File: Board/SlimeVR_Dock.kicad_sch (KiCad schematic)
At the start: 24 parts, among them J1_Control Conn_01x03_Pin, J1_MainPW USB_C_Receptacle_USB2.0_16P, J1_Prog Conn_01x03_Pin, M1 NF-A4x10 24V PWM, Q1 AO3401A, U1 ESP32-S3-WROOM-1, U2 CH224K, U3 XC6220B331MR, U4 DS18B20

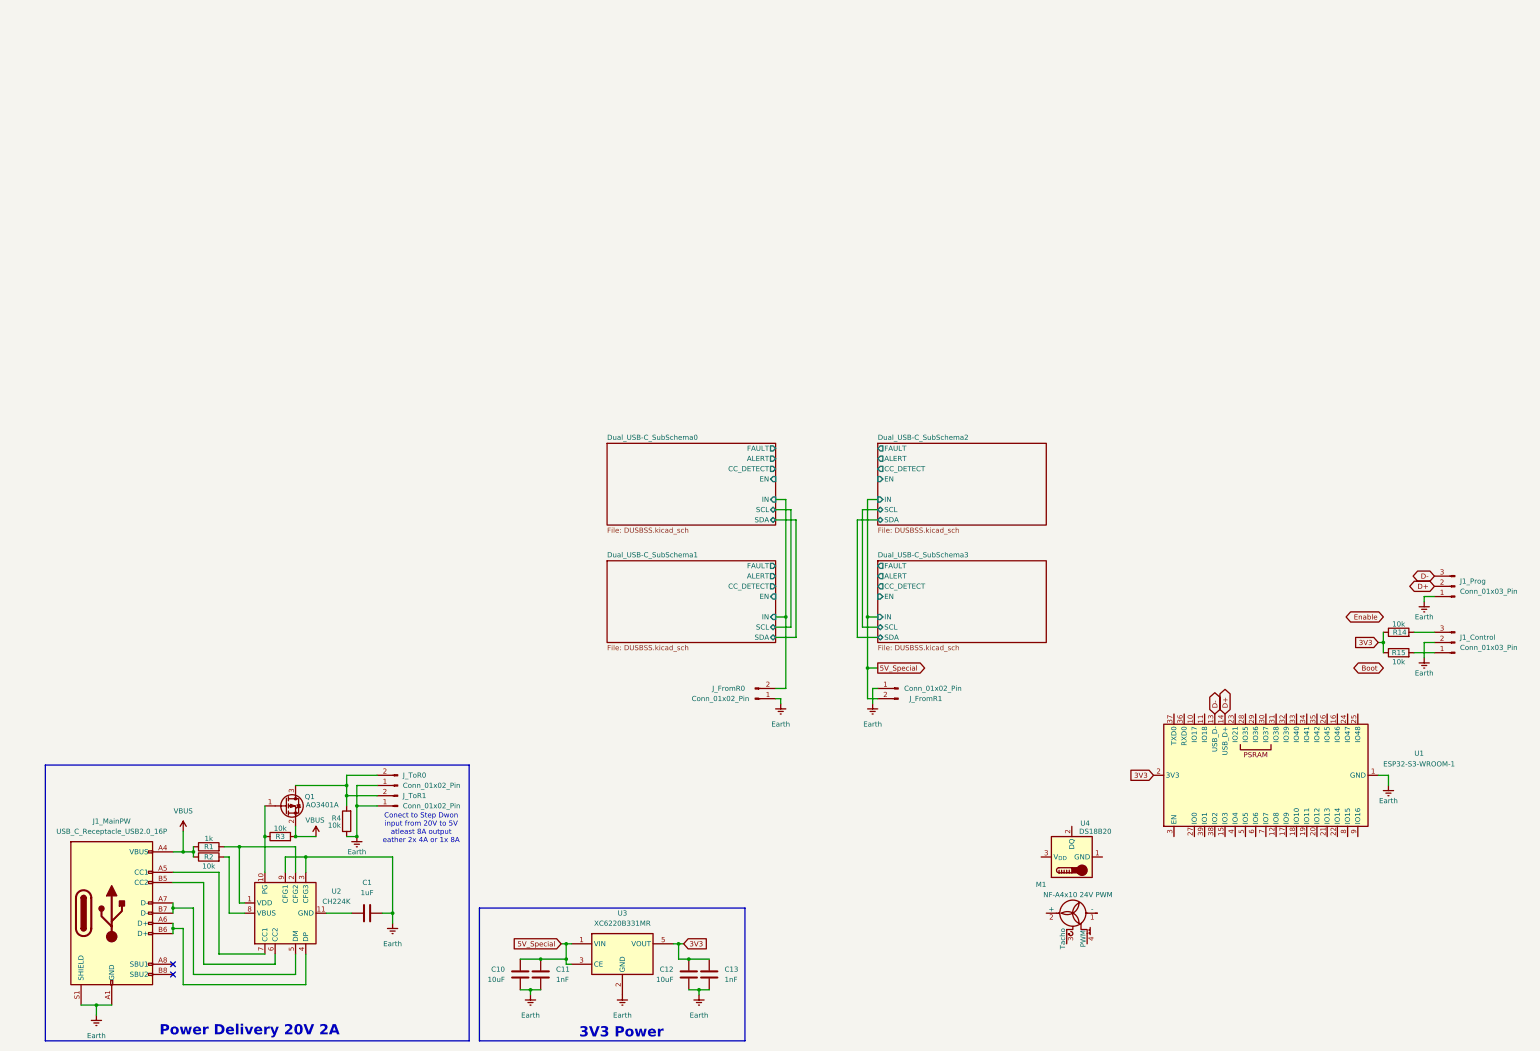
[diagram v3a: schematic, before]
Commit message: Conecting usb to esp
added in/out and out/in reistry
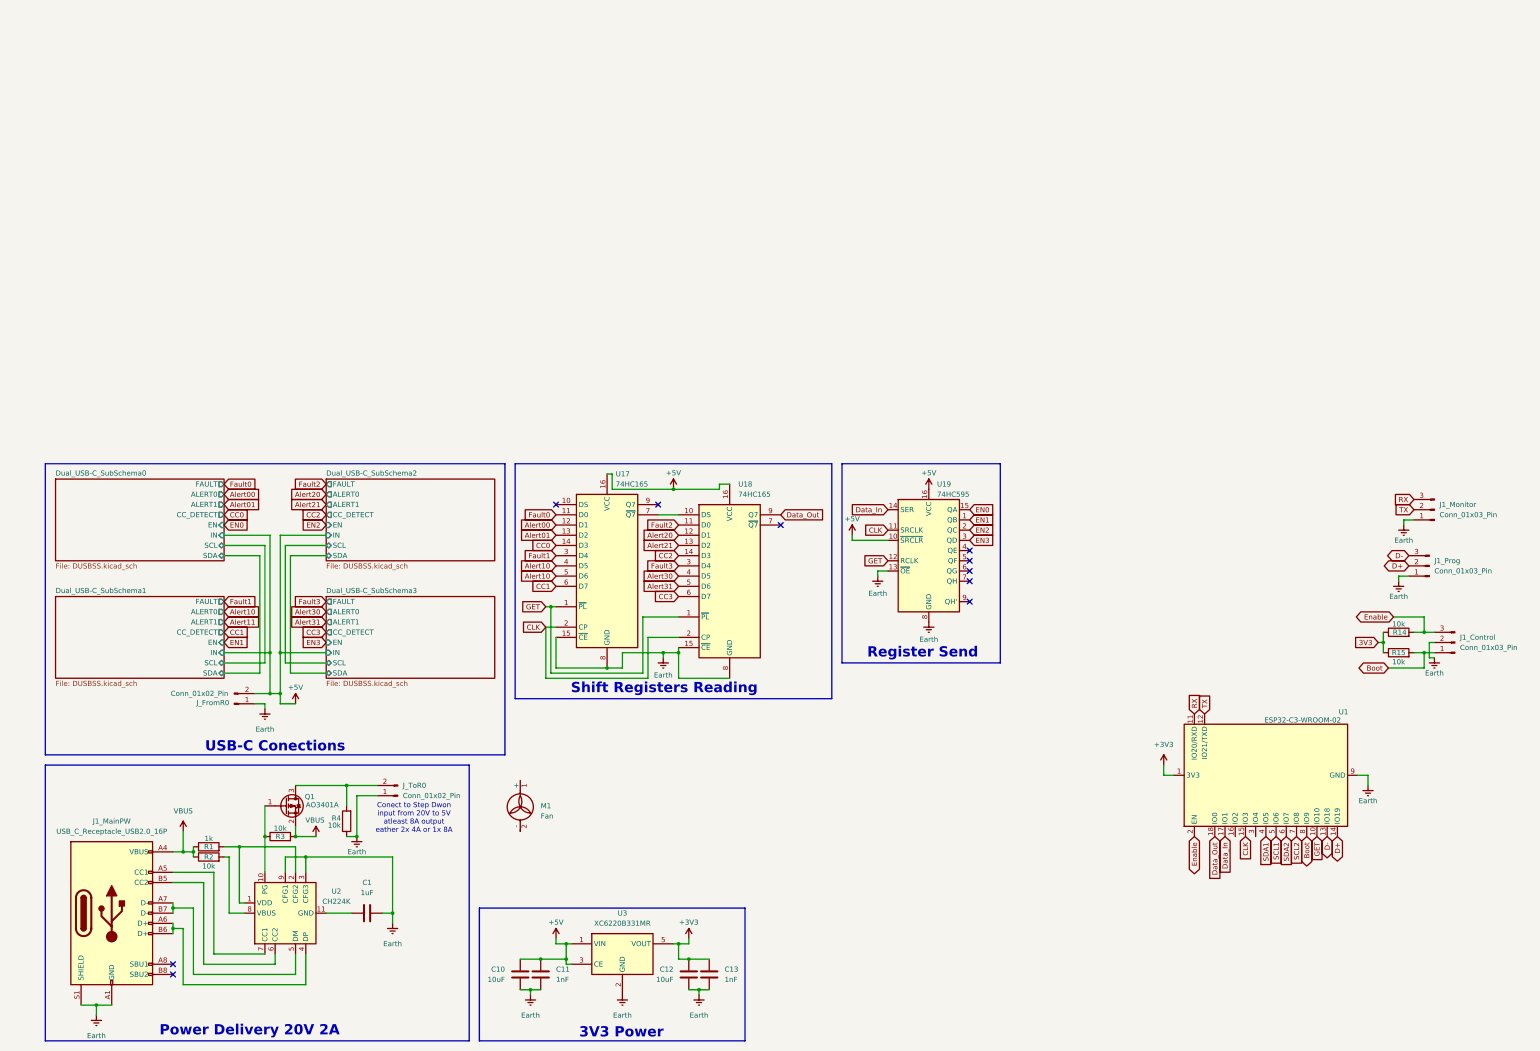
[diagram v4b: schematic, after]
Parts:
- removed J_FromR0, J_ToR1: Conn_01x02_Pin, symbol Connector:Conn_01x02_Pin
- removed M1: NF-A4x10 24V PWM, symbol Motor:Fan_4pin
- removed U1: ESP32-S3-WROOM-1, RF_Module:ESP32-S3-WROOM-1, symbol RF_Module:ESP32-S3-WROOM-1
- removed U4: DS18B20, Package_TO_SOT_THT:TO-92_Inline, symbol Sensor_Temperature:DS18B20
- added J1_Monitor: Conn_01x03_Pin, symbol Connector:Conn_01x03_Pin
- added M1: Fan, symbol Motor:Fan
- added U1: ESP32-C3-WROOM-02, RF_Module:ESP32-C3-WROOM-02, symbol RF_Module:ESP32-C3-WROOM-02
- added U17, U18: 74HC165, symbol 74xx:74HC165
- added U19: 74HC595, symbol 74xx:74HC595
- renumbered J_FromR1 to J_FromR0
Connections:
- net 3V3: no longer C12.1, C13.1, U3.5 (VOUT)
- net Boot: now also J1_Control.1 (Pin_1), R15.2, U1.8 (IO9)
- net D+: now also U1.14 (IO19)
- net D-: now also U1.13 (IO18)
- net Earth: now also J1_Monitor.1 (Pin_1), U1.19 (GND), U1.9 (GND), U17.15 (~{CE}), U17.8 (GND), U18.15 (~{CE}), U18.8 (GND), U19.13 (~{OE}), U19.8 (GND)
- net Enable: now also J1_Control.3 (Pin_3), R14.2, U1.2 (EN)
- net 5V_Special renamed +5V
- net +5V: now also U17.16 (VCC), U18.16 (VCC), U19.10 (~{SRCLR}), U19.16 (VCC)
- new net: U17.7 (~{Q7}), U18.10 (DS)
- new net +3V3: C12.1, C13.1, U1.1 (3V3), U3.5 (VOUT)
- new net Alert00: U17.12 (D1)
- new net Alert01: U17.13 (D2)
- new net Alert10: U17.4 (D5), U17.5 (D6)
- new net Alert20: U18.12 (D1)
- new net Alert21: U18.13 (D2)
- new net Alert30: U18.4 (D5)
- new net Alert31: U18.5 (D6)
- new net CC0: U17.14 (D3)
- new net CC1: U17.6 (D7)
- new net CC2: U18.14 (D3)
- new net CC3: U18.6 (D7)
- new net CLK: U1.15 (IO3), U17.2 (CP), U18.2 (CP), U19.11 (SRCLK)
- new net Data_In: U1.17 (IO1), U19.14 (SER)
- new net Data_Out: U1.18 (IO0), U18.9 (Q7)
- new net EN0: U19.15 (QA)
- new net EN1: U19.1 (QB)
- new net EN2: U19.2 (QC)
- new net EN3: U19.3 (QD)
- new net Fault0: U17.11 (D0)
- new net Fault1: U17.3 (D4)
- new net Fault2: U18.11 (D0)
- new net Fault3: U18.3 (D4)
- new net GET: U1.10 (IO10), U17.1 (~{PL}), U18.1 (~{PL}), U19.12 (RCLK)
- new net RX: J1_Monitor.3 (Pin_3), U1.11 (IO20/RXD)
- new net SCL1: U1.5 (IO6)
- new net SCL2: U1.7 (IO8)
- new net SDA1: U1.4 (IO5)
- new net SDA2: U1.6 (IO7)
- new net TX: J1_Monitor.2 (Pin_2), U1.12 (IO21/TXD)
- no-connect marks 2 -> 10
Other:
- sheet Dual_USB-C_SubSchema0 ports: added ALERT0, ALERT1; removed ALERT
- sheet Dual_USB-C_SubSchema1 ports: added ALERT0, ALERT1; removed ALERT
- sheet Dual_USB-C_SubSchema2 ports: added ALERT0, ALERT1; removed ALERT
- sheet Dual_USB-C_SubSchema3 ports: added ALERT0, ALERT1; removed ALERT
- note added: "Register Send"
- note added: "Shift Registers Reading"
- note added: "USB-C Conections"
- moved on the sheet: J1_Prog, J_FromR0, J_ToR0

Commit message: Finished Schematic
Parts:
- removed M1: Fan, symbol Motor:Fan
- added JFan1: Conn_01x04_Pin, Connector:FanPinHeader_1x04_P2.54mm_Vertical, symbol Connector:Conn_01x04_Pin
- added R23, R24: 4.7k, Resistor_SMD:R_0603_1608Metric, symbol Device:R
- C1, C10, C11, C12, C13: footprint (none) -> Capacitor_SMD:C_0603_1608Metric
- J1_Control1: renamed from J1_Control; footprint (none) -> Connector_PinHeader_2.54mm:PinHeader_1x03_P2.54mm_Vertical
- J1_MainPW1: renamed from J1_MainPW; footprint (none) -> Connector_USB:USB_C_Receptacle_GCT_USB4105-xx-A_16P_TopMnt_Horizontal
- J1_Monitor1: renamed from J1_Monitor; footprint (none) -> Connector_PinHeader_2.54mm:PinHeader_1x03_P2.54mm_Vertical
- J1_Prog1: renamed from J1_Prog; footprint (none) -> Connector_PinHeader_2.54mm:PinHeader_1x03_P2.54mm_Vertical
- J_FromR0, J_ToR0: footprint (none) -> Connector_PinHeader_2.54mm:PinHeader_1x02_P2.54mm_Vertical
- R1, R2, R3, R4: footprint (none) -> Resistor_SMD:R_0603_1608Metric
- R17: renamed from R14; footprint (none) -> Resistor_SMD:R_0603_1608Metric
- R18: renamed from R15; footprint (none) -> Resistor_SMD:R_0603_1608Metric
- U17, U18, U19: footprint (none) -> Package_SO:SOIC-16_3.9x9.9mm_P1.27mm
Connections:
- net 3V3 is gone; now on net +3V3: R17.1, R18.1
- net SDA1 is gone; now on net CLK: U1.4 (IO5)
- net +3V3: now also U17.16 (VCC), U18.16 (VCC), U19.16 (VCC), R23.2, R24.1
- net +5V: now also JFan1.2 (Pin_2); no longer U17.16 (VCC), U18.16 (VCC), U19.16 (VCC)
- net CLK: no longer U1.15 (IO3)
- net Earth: now also C1.1, U2.11 (GND), JFan1.1 (Pin_1); no longer C1.2
- net SCL: now reaches U1.3 (IO4)
- net SCL: now also R23.1
- net at R1.2, U2.1 (VDD), U2.2 (CFG2): now also C1.2
- net SCL1 renamed TACH
- net TACH: now also JFan1.3 (Pin_3)
- net SCL2: no longer names the net of U1.7 (IO8)
- net SDA2 renamed PWM
- net PWM: now also JFan1.4 (Pin_4)
- new net SDA: R24.2, U1.15 (IO3)
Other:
- sheet Dual_USB-C_SubSchema0 ports: added A00, A01, A10, A11; removed none
- sheet Dual_USB-C_SubSchema1 ports: added A00, A01, A10, A11; removed none
- sheet Dual_USB-C_SubSchema2 ports: added A00, A01, A10, A11; removed none
- sheet Dual_USB-C_SubSchema3 ports: added A00, A01, A10, A11; removed none
- note added: "Conect to Step Dwon input from 20V to 5V atleast 8A+ output"
- note added: "Dev pins"
- note added: "I recomend XL4016, 9A"
- note added: "MCU"
- note added: "Power Delivery 20V 3A"
- note removed: "Conect to Step Dwon input from 20V to 5V atleast 8A output eather 2x 4A or 1x 8A"
- note removed: "Power Delivery 20V 2A"
- moved on the sheet: C1, C10, C11, C12, C13, J1_Control1, J1_MainPW1, J1_Monitor1, J1_Prog1, J_FromR0, J_ToR0, Q1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

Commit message: Updavení USB-C
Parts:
- added BZ1: Buzzer, Buzzer_Beeper:Buzzer_12x9.5RM7.6, symbol Device:Buzzer
- added D1: 1N4148, Diode_SMD:D_0603_1608Metric, symbol Device:D
- added J1Temp1: Conn_01x05_Pin, Connector_PinHeader_2.54mm:PinHeader_1x05_P2.54mm_Vertical, symbol Connector:Conn_01x05_Pin
- added Q6: BC817, Package_TO_SOT_SMD:SOT-23, symbol Transistor_BJT:BC817
- added R33: 1k, Resistor_SMD:R_0603_1608Metric, symbol Device:R
- renumbered JFan1 to J1Fan1
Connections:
- net +3V3: now also J1Temp1.1 (Pin_1)
- net +5V: now also BZ1.1 (+), D1.1 (K)
- net Earth: now also J1Temp1.3 (Pin_3), Q6.2 (E)
- net SCL: now also J1Temp1.2 (Pin_2)
- net SDA: now also J1Temp1.4 (Pin_4)
- net BZ: now reaches U19.4 (QE)
- net BZ: now also R33.1
- new net: Q6.1 (B), R33.2
- new net: BZ1.2 (-), D1.2 (A), Q6.3 (C)
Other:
- note added: "3V3 Power Generator"
- note added: "I use TC74A0 in TO-220 footprint"
- note added: "Shift Register Send"
- note added: "StepDwon Fan Sensor Conector"
- note added: "Tempeture Sensor Conector"
- note added: "User Warning"
- note removed: "3V3 Power"
- note removed: "Register Send"
- moved on the sheet: J1Fan1

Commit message: Custom StepDown
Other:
- added sheet StepDown (StepDown.kicad_sch)
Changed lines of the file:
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@@
+	)
+	(sheet
+		(at 106.68 114.3)
+		(size 12.7 8.89)
+		(exclude_from_sim no)
+		(in_bom yes)
+		(on_board yes)
+		(dnp no)
+		(stroke
+			(width 0.1524)
+			(type solid)
+		)
+		(fill
+			(color 0 0 0 0.0000)
+		)
+		(property "Sheetname" "StepDown"
+			(at 106.68 113.5884 0)
+			(effects
+				(font
+					(size 1.27 1.27)
+				)
+				(justify left bottom)
+			)
+		)
+		(property "Sheetfile" "StepDown.kicad_sch"
+			(at 105.41 123.698 0)
+			(effects
+				(font
+					(size 1.27 1.27)
+				)
+				(justify left top)
+			)
+		)
+		(instances
+			(project "SlimeVR_Dock"
+				(path "/06ff9557-1f9b-4670-8a34-bb7684a016dd"
+					(page "14")
+				)
+			)
+		)
 	)
 	(sheet

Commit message: minority upravy
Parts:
- removed J_FromR0, J_ToR0: Conn_01x02_Pin, Connector_PinHeader_2.54mm:PinHeader_1x02_P2.54mm_Vertical, symbol Connector:Conn_01x02_Pin
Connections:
- net StepDown/Vin: now reaches Q1.3 (D), R4.2
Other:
- sheet StepDown ports: added Vin, Vout; removed none
- note removed: "Conect to Step Dwon input from 20V to 5V atleast 8A+ output"
- note removed: "I recomend XL4016, 9A"
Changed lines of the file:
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@@
 		)
 	)
-	(text "I recomend XL4016, 9A"
-		(exclude_from_sim no)
-		(at 121.158 110.236 0)
-		(effects
-			(font
-				(size 1.27 1.27)
-			)
-		)
-	)
 	(text "I use TC74A0 in TO-220 footprint"
 		(exclude_from_sim no)
@@
 		)
 	)
-	(text "Conect to Step Dwon \ninput from 20V to 5V\natleast 8A+ output\n\n"
-		(exclude_from_sim no)
-		(at 121.412 105.664 0)
-		(effects
-			(font
-				(size 1.27 1.27)
-			)
-		)
-	)
 	(text "Shift Register Send"
 		(exclude_from_sim no)
@@
 	)
 	(junction
+		(at 96.52 97.79)
+		(diameter 0)
+		(color 0 0 0 0)
+	)
+	(junction
 		(at 73.66 64.77)
 		(diameter 0)
@@
 	)
 	(junction
-		(at 96.52 97.79)
-		(diameter 0)
-		(color 0 0 0 0)
-	)
-	(junction
 		(at 233.68 87.63)
 		(diameter 0)
@@
 		(color 0 0 0 0)
 	)
-	(junction
-		(at 99.06 110.49)
-		(diameter 0)
-		(color 0 0 0 0)
-	)
 	(no_connect
 		(at 167.64 104.14)
@@
 	(wire
 		(pts
-			(xy 73.66 80.01) (xy 71.12 80.01)
-		)
-		(stroke
-			(width 0)
-			(type default)
-		)
-	)
-	(wire
-		(pts
 			(xy 163.83 138.43) (xy 163.83 142.24)
 		)
@@
 	(wire
 		(pts
+			(xy 115.57 97.79) (xy 114.3 97.79)
+		)
+		(stroke
+			(width 0)
+			(type default)
+		)
+	)
+	(wire
+		(pts
 			(xy 172.72 64.77) (xy 172.72 63.5)
 		)
@@
 		)
 	)
+	(wire
+		(pts
+			(xy 101.6 97.79) (xy 96.52 97.79)
+		)
+		(stroke
+			(width 0)
+			(type default)
+		)
+	)
 	(bus
 		(pts
@@
 	(wire
 		(pts
-			(xy 99.06 100.33) (xy 99.06 110.49)
-		)
-		(stroke
-			(width 0)
-			(type default)
-		)
-	)
-	(wire
-		(pts
 			(xy 194.31 106.68) (xy 193.04 106.68)
 		)
@@
 	(wire
 		(pts
-			(xy 110.49 100.33) (xy 99.06 100.33)
-		)
-		(stroke
-			(width 0)
-			(type default)
-		)
-	)
-	(wire
-		(pts
 			(xy 77.47 40.64) (xy 77.47 44.45)
 		)
@@
 	(wire
 		(pts
-			(xy 96.52 97.79) (xy 110.49 97.79)
-		)
-		(stroke
-			(width 0)
-			(type default)
-		)
-	)
-	(wire
-		(pts
 			(xy 189.23 119.38) (xy 193.04 119.38)
 		)
@@
 	(wire
 		(pts
-			(xy 73.66 80.01) (xy 73.66 81.28)
-		)
-		(stroke
-			(width 0)
-			(type default)
-		)
-	)
-	(wire
-		(pts
 			(xy 26.67 41.91) (xy 26.67 43.18)
 		)
@@
 		)
 	)
+	(global_label "5VStepDwon"
+		(shape input)
+		(at 71.12 77.47 180)
+		(fields_autoplaced yes)
+		(effects
+			(font
+				(size 1.27 1.27)
+			)
+			(justify right)
+		)
+		(property "Intersheetrefs" "${INTERSHEET_REFS}"
+			(at 56.7654 77.47 0)
+			(effects
+				(font
+					(size 1.27 1.27)
+				)
+				(justify right)
+				(hide yes)
+			)
+		)
+	)
 	(global_label "TACH"
 		(shape input)
@@
 		)
 	)
+	(global_label "5VStepDwon"
+		(shape input)
+		(at 115.57 97.79 0)
+		(fields_autoplaced yes)
+		(effects
+			(font
+				(size 1.27 1.27)
+			)
+			(justify left)
+		)
+		(property "Intersheetrefs" "${INTERSHEET_REFS}"
+			(at 129.9246 97.79 0)
+			(effects
+				(font
+					(size 1.27 1.27)
+				)
+				(justify left)
+				(hide yes)
+			)
+		)
+	)
 	(global_label "Data_Out"
 		(shape input)
@@
 	)
 	(symbol
-		(lib_id "Connector:Conn_01x02_Pin")
-		(at 66.04 80.01 0)
-		(mirror x)
-		(unit 1)
-		(exclude_from_sim no)
-		(in_bom yes)
-		(on_board yes)
-		(dnp no)
-		(property "Reference" "J_FromR0"
-			(at 60.706 79.756 0)
-			(effects
-				(font
-					(size 1.27 1.27)
-				)
-			)
-		)
-		(property "Value" "Conn_01x02_Pin"
-			(at 57.404 77.47 0)
-			(effects
-				(font
-					(size 1.27 1.27)
-				)
-			)
-		)
-		(property "Footprint" "Connector_PinHeader_2.54mm:PinHeader_1x02_P2.54mm_Vertical"
-			(at 66.04 80.01 0)
-			(effects
-				(font
-					(size 1.27 1.27)
-				)
-				(hide yes)
-			)
-		)
-		(property "Datasheet" "~"
-			(at 66.04 80.01 0)
-			(effects
-				(font
-					(size 1.27 1.27)
-				)
-				(hide yes)
-			)
-		)
-		(property "Description" "Generic connector, single row, 01x02, script generated"
-			(at 66.04 80.01 0)
-			(effects
-				(font
-					(size 1.27 1.27)
-				)
-				(hide yes)
-			)
-		)
-		(pin "2"
-		)
-		(pin "1"
-		)
-		(instances
-			(project "SlimeVR_Dock"
-				(path "/06ff9557-1f9b-4670-8a34-bb7684a016dd"
-					(reference "J_FromR0")
-					(unit 1)
-				)
-			)
-		)
-	)
-	(symbol
 		(lib_id "power:Earth")
 		(at 99.06 110.49 0)
@@
 	(symbol
 		(lib_id "power:Earth")
-		(at 73.66 81.28 0)
-		(unit 1)
-		(exclude_from_sim no)
-		(in_bom yes)
-		(on_board yes)
-		(dnp no)
-		(property "Reference" "#PWR027"
-			(at 73.66 87.63 0)
-			(effects
-				(font
-					(size 1.27 1.27)
-				)
-				(hide yes)
-			)
-		)
-		(property "Value" "Earth"
-			(at 73.66 85.344 0)
-			(effects
-				(font
-					(size 1.27 1.27)
-				)
-			)
-		)
-		(property "Footprint" ""
-			(at 73.66 81.28 0)
-			(effects
-				(font
-					(size 1.27 1.27)
-				)
-				(hide yes)
-			)
-		)
-		(property "Datasheet" "~"
-			(at 73.66 81.28 0)
-			(effects
-				(font
-					(size 1.27 1.27)
-				)
-				(hide yes)
-			)
-		)
-		(property "Description" "Power symbol creates a global label with name \"Earth\""
-			(at 73.66 81.28 0)
-			(effects
-				(font
-					(size 1.27 1.27)
-				)
-				(hide yes)
-			)
-		)
-		(pin "1"
-		)
-		(instances
-			(project "SlimeVR_Dock"
-				(path "/06ff9557-1f9b-4670-8a34-bb7684a016dd"
-					(reference "#PWR027")
-					(unit 1)
-				)
-			)
-		)
-	)
-	(symbol
-		(lib_id "power:Earth")
 		(at 172.72 64.77 0)
 		(unit 1)
@@
 	)
 	(symbol
-		(lib_id "Connector:Conn_01x02_Pin")
-		(at 115.57 100.33 180)
-		(unit 1)
-		(exclude_from_sim no)
-		(in_bom yes)
-		(on_board yes)
-		(dnp no)
-		(fields_autoplaced yes)
-		(property "Reference" "J_ToR0"
-			(at 116.84 97.7899 0)
-			(effects
-				(font
-					(size 1.27 1.27)
-				)
-				(justify right)
-			)
-		)
-		(property "Value" "Conn_01x02_Pin"
-			(at 116.84 100.3299 0)
-			(effects
-				(font
-					(size 1.27 1.27)
-				)
-				(justify right)
-			)
-		)
-		(property "Footprint" "Connector_PinHeader_2.54mm:PinHeader_1x02_P2.54mm_Vertical"
-			(at 115.57 100.33 0)
-			(effects
-				(font
-					(size 1.27 1.27)
-				)
-				(hide yes)
-			)
-		)
-		(property "Datasheet" "~"
-			(at 115.57 100.33 0)
-			(effects
-				(font
-					(size 1.27 1.27)
-				)
-				(hide yes)
-			)
-		)
-		(property "Description" "Generic connector, single row, 01x02, script generated"
-			(at 115.57 100.33 0)
-			(effects
-				(font
-					(size 1.27 1.27)
-				)
-				(hide yes)
-			)
-		)
-		(pin "2"
-		)
-		(pin "1"
-		)
-		(instances
-			(project "SlimeVR_Dock"
-				(path "/06ff9557-1f9b-4670-8a34-bb7684a016dd"
-					(reference "J_ToR0")
-					(unit 1)
-				)
-			)
-		)
-	)
-	(symbol
 		(lib_id "power:+5V")
 		(at 237.49 67.31 0)
@@
 	)
 	(sheet
-		(at 106.68 114.3)
-		(size 12.7 8.89)
+		(at 101.6 95.25)
+		(size 12.7 5.08)
 		(exclude_from_sim no)
 		(in_bom yes)
@@
 		)
 		(property "Sheetname" "StepDown"
-			(at 106.68 113.5884 0)
+			(at 101.6 94.5384 0)
 			(effects
 				(font
@@
 		)
 		(property "Sheetfile" "StepDown.kicad_sch"
-			(at 105.41 123.698 0)
+			(at 98.806 100.838 0)
 			(effects
 				(font
@@
 			)
 		)
+		(pin "Vin" input
+			(at 101.6 97.79 180)
+			(effects
+				(font
+					(size 1.27 1.27)
+				)
+				(justify left)
+			)
+		)
+		(pin "Vout" input
+			(at 114.3 97.79 0)
+			(effects
+				(font
+					(size 1.27 1.27)
+				)
+				(justify right)
+			)
+		)
